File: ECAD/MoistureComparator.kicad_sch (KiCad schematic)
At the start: 14 parts, among them U1 LM393

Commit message: pcb layout has started, still ned to make 5V to 3.3V power supply, add dip switch do individually control input power of each switch, 5V or 12V
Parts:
- U1: value LM393 -> LM293; footprint Potentiometer_SMD:Potentiometer_Bourns_TC33X_Vertical -> Package_SO:SO-8_3.9x4.9mm_P1.27mm
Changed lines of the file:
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@@
       (effects (font (size 1.27 1.27)) (justify left))
     )
-    (property "Value" "LM393" (id 1) (at 97.9932 95.123 0)
+    (property "Value" "LM293" (id 1) (at 97.9932 95.123 0)
       (effects (font (size 1.27 1.27)) (justify left))
     )
-    (property "Footprint" "Potentiometer_SMD:Potentiometer_Bourns_TC33X_Vertical" (id 2) (at 99.06 93.98 0)
+    (property "Footprint" "Package_SO:SO-8_3.9x4.9mm_P1.27mm" (id 2) (at 99.06 93.98 0)
       (effects (font (size 1.27 1.27)) hide)
     )
-    (property "Datasheet" "http://www.ti.com/lit/ds/symlink/lm393.pdf" (id 3) (at 99.06 93.98 0)
+    (property "Datasheet" "http://www.ti.com/lit/ds/symlink/LM293.pdf" (id 3) (at 99.06 93.98 0)
       (effects (font (size 1.27 1.27)) hide)
     )
@@
     (in_bom yes) (on_board yes)
     (property "Reference" "U1" (id 0) (at 175.26 65.6082 0))
-    (property "Value" "LM393" (id 1) (at 175.26 67.9196 0))
-    (property "Footprint" "Potentiometer_SMD:Potentiometer_Bourns_TC33X_Vertical" (id 2) (at 175.26 74.93 0)
+    (property "Value" "LM293" (id 1) (at 175.26 67.9196 0))
+    (property "Footprint" "Package_SO:SO-8_3.9x4.9mm_P1.27mm" (id 2) (at 175.26 74.93 0)
       (effects (font (size 1.27 1.27)) hide)
     )
-    (property "Datasheet" "http://www.ti.com/lit/ds/symlink/lm393.pdf" (id 3) (at 175.26 74.93 0)
+    (property "Datasheet" "http://www.ti.com/lit/ds/symlink/LM293.pdf" (id 3) (at 175.26 74.93 0)
       (effects (font (size 1.27 1.27)) hide)
     )
@@
     (in_bom yes) (on_board yes)
     (property "Reference" "U1" (id 0) (at 175.26 115.1382 0))
-    (property "Value" "LM393" (id 1) (at 175.26 117.4496 0))
-    (property "Footprint" "Potentiometer_SMD:Potentiometer_Bourns_TC33X_Vertical" (id 2) (at 175.26 124.46 0)
+    (property "Value" "LM293" (id 1) (at 175.26 117.4496 0))
+    (property "Footprint" "Package_SO:SO-8_3.9x4.9mm_P1.27mm" (id 2) (at 175.26 124.46 0)
       (effects (font (size 1.27 1.27)) hide)
     )
-    (property "Datasheet" "http://www.ti.com/lit/ds/symlink/lm393.pdf" (id 3) (at 175.26 124.46 0)
+    (property "Datasheet" "http://www.ti.com/lit/ds/symlink/LM293.pdf" (id 3) (at 175.26 124.46 0)
       (effects (font (size 1.27 1.27)) hide)
     )

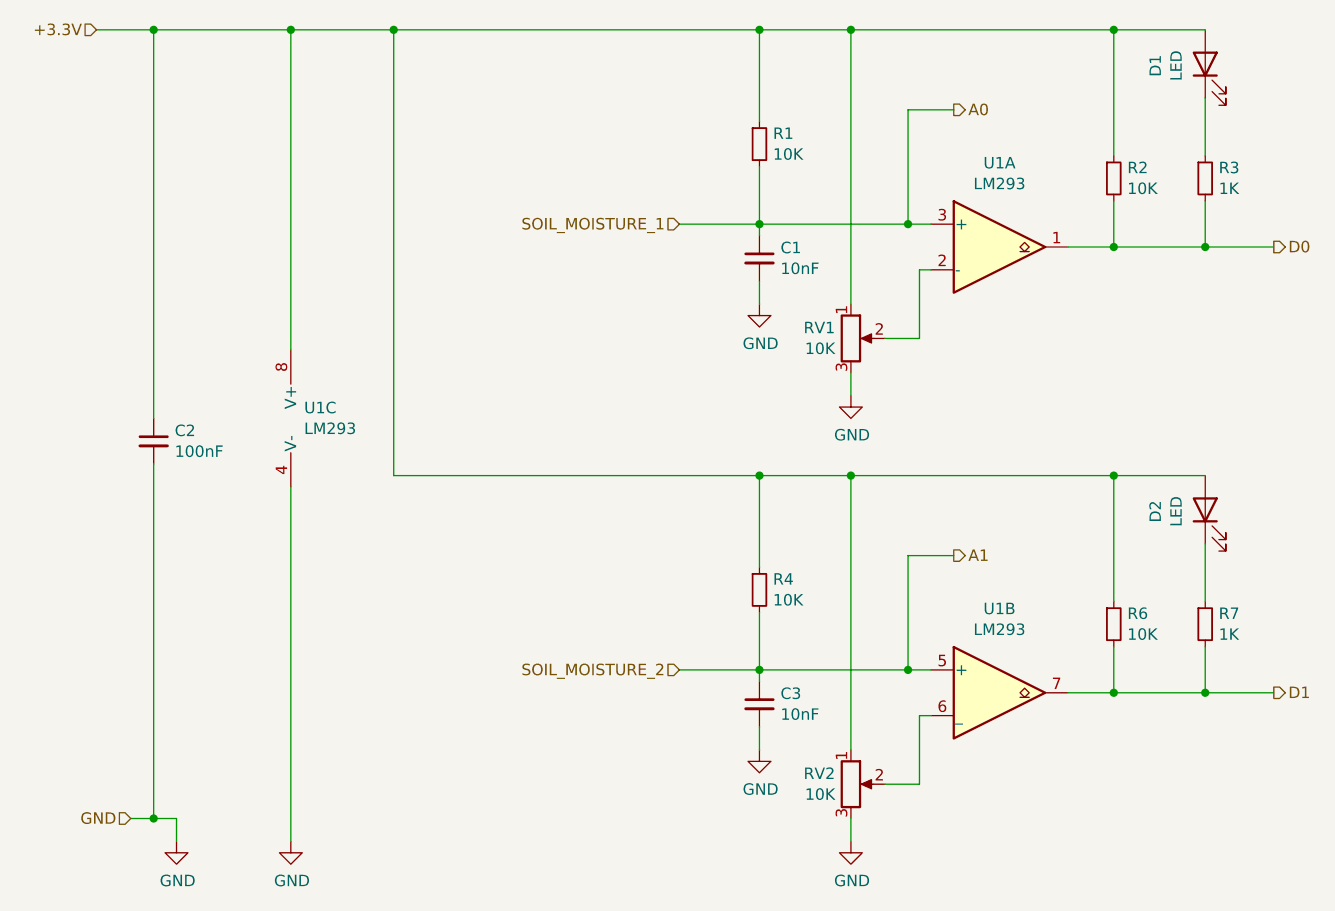
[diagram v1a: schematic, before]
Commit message: finishing up pcb, only billonly bill of materials need to be done to be compatible with lc from jlcpcb
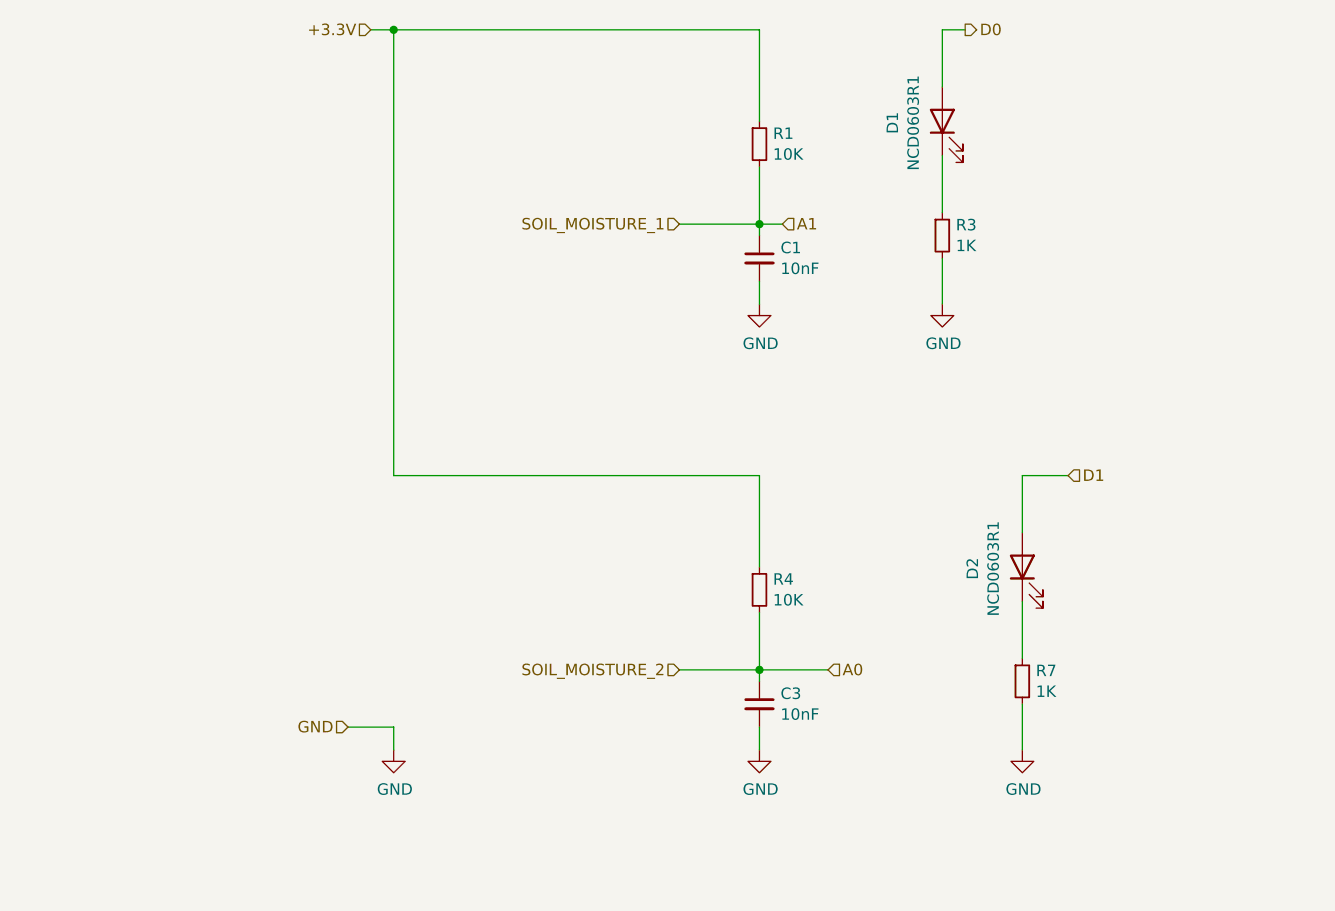
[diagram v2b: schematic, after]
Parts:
- removed C2: 100nF, Capacitor_SMD:C_0603_1608Metric, symbol Device:C_Small
- removed R2, R6: 10K, Resistor_SMD:R_0603_1608Metric, symbol Device:R_Small
- removed RV1, RV2: 10K, Potentiometer_SMD:Potentiometer_Bourns_TC33X_Vertical, symbol Device:R_Potentiometer
- removed U1: LM293, Package_SO:SO-8_3.9x4.9mm_P1.27mm, symbol Comparator:LM393
- D1, D2: value LED -> NCD0603R1; footprint Resistor_SMD:R_0603_1608Metric -> LED_SMD:LED_0603_1608Metric
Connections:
- net +3.3V: no longer D1.2 (A), D2.2 (A)
- net A0: now also C3.1, R4.2; no longer C1.1, R1.2
- net A1: now also C1.1, R1.2; no longer C3.1, R4.2
- net D0: now also D1.2 (A); no longer R3.2
- net D1: now also D2.2 (A); no longer R7.2
- net GND: now also R3.2, R7.2
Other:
- moved on the sheet: D1, D2, R3, R7

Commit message: BOM fixed, ready to order
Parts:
- C1, C3: Manufacturer (none) -> CCTC; Manufacturer Number (none) -> TCC0603X7R103M500CT
- D1, D2: Manufacturer (none) -> Foshan NationStar Optoelectronics; Manufacturer Number (none) -> NCD0603R1
- R1, R4: Manufacturer (none) -> UNI-ROYAL(Uniroyal Elec); Manufacturer Number (none) -> 0603WAF1002T5E
- R3, R7: Manufacturer (none) -> FH(Guangdong Fenghua Advanced Tech); Manufacturer Number (none) -> RS-03K1001FT
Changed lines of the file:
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@@
       (effects (font (size 1.27 1.27)) hide)
     )
-    (property "Datasheet" "~" (id 3) (at 148.59 63.5 0)
+    (property "Datasheet" "https://datasheet.lcsc.com/lcsc/1811062009_UNI-ROYAL-Uniroyal-Elec-0603WAF1002T5E_C25804.pdf" (id 3) (at 148.59 63.5 0)
+      (effects (font (size 1.27 1.27)) hide)
+    )
+    (property "Manufacturer" "UNI-ROYAL(Uniroyal Elec)" (id 4) (at 148.59 63.5 0)
+      (effects (font (size 1.27 1.27)) hide)
+    )
+    (property "Manufacturer Number" "0603WAF1002T5E" (id 5) (at 148.59 63.5 0)
       (effects (font (size 1.27 1.27)) hide)
     )
@@
       (effects (font (size 1.27 1.27)) hide)
     )
-    (property "Datasheet" "~" (id 3) (at 148.59 113.03 0)
+    (property "Datasheet" "https://datasheet.lcsc.com/lcsc/1811062009_UNI-ROYAL-Uniroyal-Elec-0603WAF1002T5E_C25804.pdf" (id 3) (at 148.59 113.03 0)
+      (effects (font (size 1.27 1.27)) hide)
+    )
+    (property "Manufacturer" "UNI-ROYAL(Uniroyal Elec)" (id 4) (at 148.59 113.03 0)
+      (effects (font (size 1.27 1.27)) hide)
+    )
+    (property "Manufacturer Number" "0603WAF1002T5E" (id 5) (at 148.59 113.03 0)
       (effects (font (size 1.27 1.27)) hide)
     )
@@
       (effects (font (size 1.27 1.27)) hide)
     )
-    (property "Datasheet" "~" (id 3) (at 168.91 73.66 0)
+    (property "Datasheet" "https://datasheet.lcsc.com/lcsc/1811011704_FH-Guangdong-Fenghua-Advanced-Tech-RS-03K1001FT_C115325.pdf" (id 3) (at 168.91 73.66 0)
+      (effects (font (size 1.27 1.27)) hide)
+    )
+    (property "Manufacturer" "FH(Guangdong Fenghua Advanced Tech)" (id 4) (at 168.91 73.66 0)
+      (effects (font (size 1.27 1.27)) hide)
+    )
+    (property "Manufacturer Number" "RS-03K1001FT" (id 5) (at 168.91 73.66 0)
       (effects (font (size 1.27 1.27)) hide)
     )
@@
       (effects (font (size 1.27 1.27)) hide)
     )
-    (property "Datasheet" "~" (id 3) (at 177.8 123.19 0)
+    (property "Datasheet" "https://datasheet.lcsc.com/lcsc/1811011704_FH-Guangdong-Fenghua-Advanced-Tech-RS-03K1001FT_C115325.pdf" (id 3) (at 177.8 123.19 0)
+      (effects (font (size 1.27 1.27)) hide)
+    )
+    (property "Manufacturer" "FH(Guangdong Fenghua Advanced Tech)" (id 4) (at 177.8 123.19 0)
+      (effects (font (size 1.27 1.27)) hide)
+    )
+    (property "Manufacturer Number" "RS-03K1001FT" (id 5) (at 177.8 123.19 0)
       (effects (font (size 1.27 1.27)) hide)
     )
@@
       (effects (font (size 1.27 1.27)) hide)
     )
-    (property "Datasheet" "~" (id 3) (at 148.59 76.2 0)
+    (property "Datasheet" "https://datasheet.lcsc.com/lcsc/1811071519_Darfon-Elec-C0603X7R103METS_C312126.pdf" (id 3) (at 148.59 76.2 0)
+      (effects (font (size 1.27 1.27)) hide)
+    )
+    (property "Manufacturer" "CCTC" (id 4) (at 148.59 76.2 0)
+      (effects (font (size 1.27 1.27)) hide)
+    )
+    (property "Manufacturer Number" "TCC0603X7R103M500CT" (id 5) (at 148.59 76.2 0)
       (effects (font (size 1.27 1.27)) hide)
     )
@@
       (effects (font (size 1.27 1.27)) hide)
     )
-    (property "Datasheet" "~" (id 3) (at 148.59 125.73 0)
+    (property "Datasheet" "https://datasheet.lcsc.com/lcsc/1811071519_Darfon-Elec-C0603X7R103METS_C312126.pdf" (id 3) (at 148.59 125.73 0)
+      (effects (font (size 1.27 1.27)) hide)
+    )
+    (property "Manufacturer" "CCTC" (id 4) (at 148.59 125.73 0)
+      (effects (font (size 1.27 1.27)) hide)
+    )
+    (property "Manufacturer Number" "TCC0603X7R103M500CT" (id 5) (at 148.59 125.73 0)
       (effects (font (size 1.27 1.27)) hide)
     )
@@
       (effects (font (size 1.27 1.27)) hide)
     )
-    (property "Datasheet" "~" (id 3) (at 168.91 60.96 0)
+    (property "Datasheet" "https://datasheet.lcsc.com/lcsc/2008201032_Foshan-NationStar-Optoelectronics-NCD0603R1_C84263.pdf" (id 3) (at 168.91 60.96 0)
+      (effects (font (size 1.27 1.27)) hide)
+    )
+    (property "Manufacturer" "	Foshan NationStar Optoelectronics" (id 4) (at 168.91 60.96 0)
+      (effects (font (size 1.27 1.27)) hide)
+    )
+    (property "Manufacturer Number" "NCD0603R1" (id 5) (at 168.91 60.96 0)
       (effects (font (size 1.27 1.27)) hide)
     )
@@
       (effects (font (size 1.27 1.27)) hide)
     )
-    (property "Datasheet" "~" (id 3) (at 177.8 110.49 0)
+    (property "Datasheet" "https://datasheet.lcsc.com/lcsc/2008201032_Foshan-NationStar-Optoelectronics-NCD0603R1_C84263.pdf" (id 3) (at 177.8 110.49 0)
       (effects (font (size 1.27 1.27)) hide)
     )
+    (property "Manufacturer" "	Foshan NationStar Optoelectronics" (id 4) (at 177.8 110.49 0)
+      (effects (font (size 1.27 1.27)) hide)
+    )
+    (property "Manufacturer Number" "NCD0603R1" (id 5) (at 177.8 110.49 0)
+      (effects (font (size 1.27 1.27)) hide)
+    )

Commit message: adding production and step files
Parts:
- C1, C3, D1, D2, R1, R3, R4, R7: Package (none) -> 0603
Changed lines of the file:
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@@
+      (effects (font (size 1.27 1.27)) hide)
+    )
+    (property "Package" "0603" (id 4) (at 148.59 63.5 0)
       (effects (font (size 1.27 1.27)) hide)
     )
@@
       (effects (font (size 1.27 1.27)) hide)
     )
+    (property "Package" "0603" (id 4) (at 148.59 113.03 0)
+      (effects (font (size 1.27 1.27)) hide)
+    )
     (pin "1")
     (pin "2")
@@
     )
     (property "Manufacturer Number" "RS-03K1001FT" (id 5) (at 168.91 73.66 0)
+      (effects (font (size 1.27 1.27)) hide)
+    )
+    (property "Package" "0603" (id 4) (at 168.91 73.66 0)
       (effects (font (size 1.27 1.27)) hide)
     )
@@
       (effects (font (size 1.27 1.27)) hide)
     )
+    (property "Package" "0603" (id 4) (at 177.8 123.19 0)
+      (effects (font (size 1.27 1.27)) hide)
+    )
     (pin "1")
     (pin "2")
@@
     )
     (property "Manufacturer Number" "TCC0603X7R103M500CT" (id 5) (at 148.59 76.2 0)
+      (effects (font (size 1.27 1.27)) hide)
+    )
+    (property "Package" "0603" (id 4) (at 148.59 76.2 0)
       (effects (font (size 1.27 1.27)) hide)
     )
@@
       (effects (font (size 1.27 1.27)) hide)
     )
+    (property "Package" "0603" (id 4) (at 148.59 125.73 0)
+      (effects (font (size 1.27 1.27)) hide)
+    )
     (pin "1")
     (pin "2")
@@
     )
     (property "Manufacturer Number" "NCD0603R1" (id 5) (at 168.91 60.96 0)
+      (effects (font (size 1.27 1.27)) hide)
+    )
+    (property "Package" "0603" (id 4) (at 168.91 60.96 0)
       (effects (font (size 1.27 1.27)) hide)
     )
@@
       (effects (font (size 1.27 1.27)) hide)
     )
+    (property "Package" "0603" (id 4) (at 177.8 110.49 0)
+      (effects (font (size 1.27 1.27)) hide)
+    )
